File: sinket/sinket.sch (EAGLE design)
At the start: 16 parts, among them IC1 ATTINY85-20PU

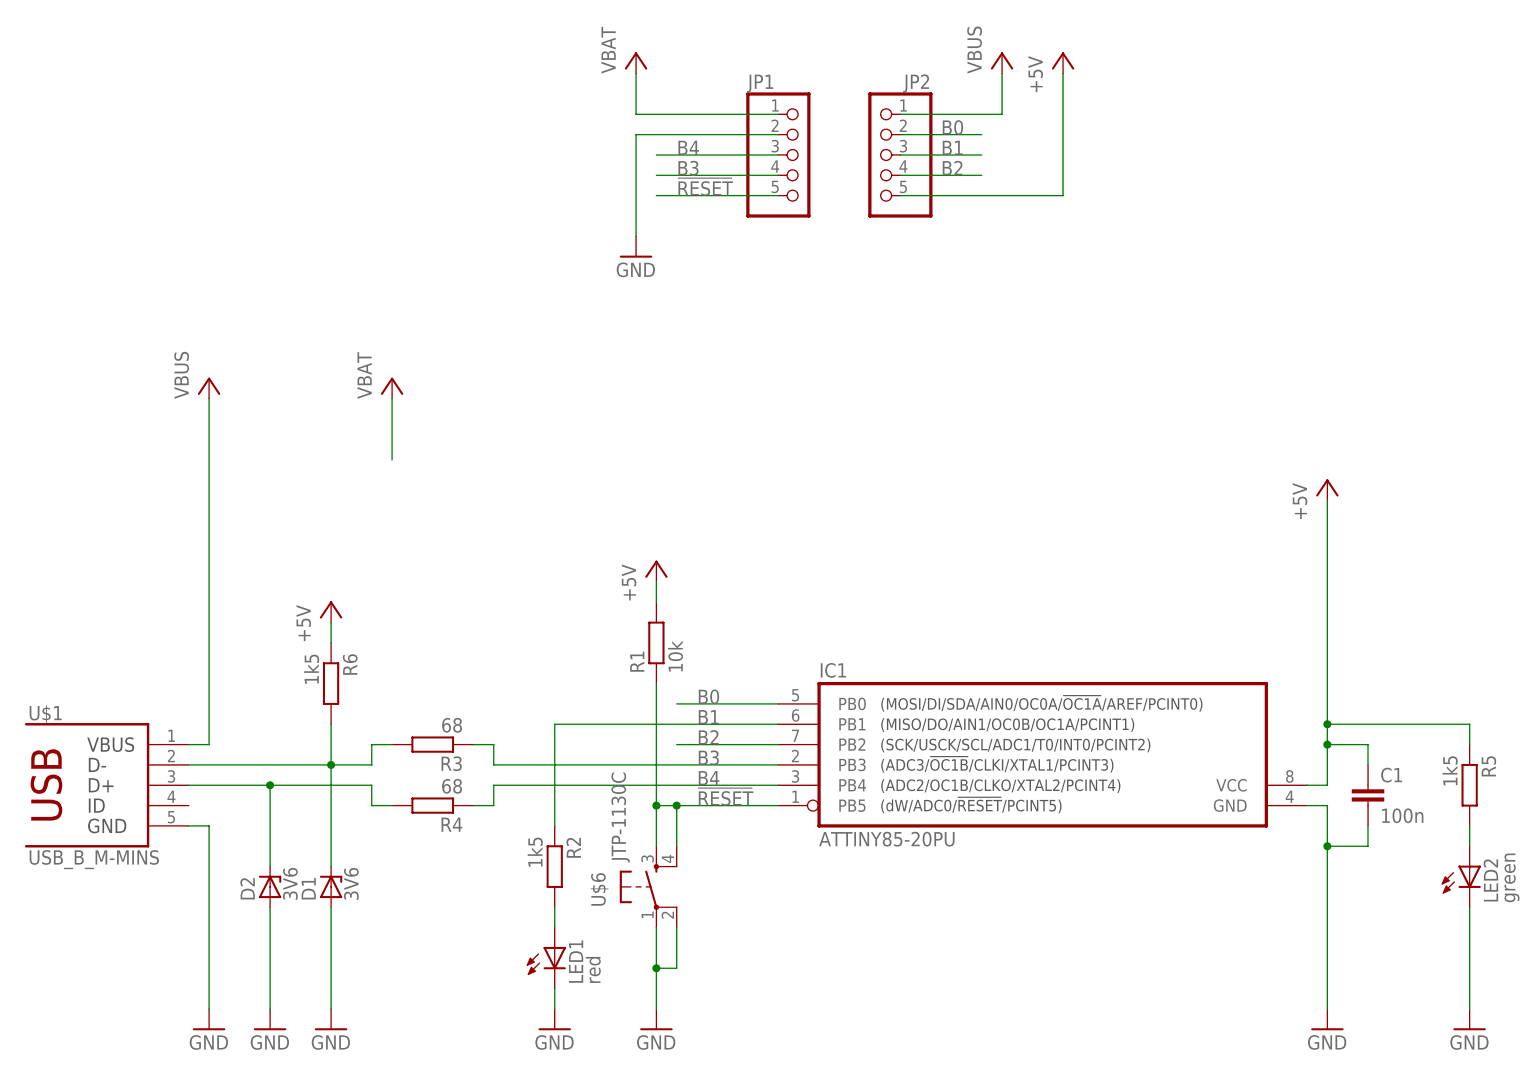
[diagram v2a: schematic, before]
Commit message: add remaining parts to schematic
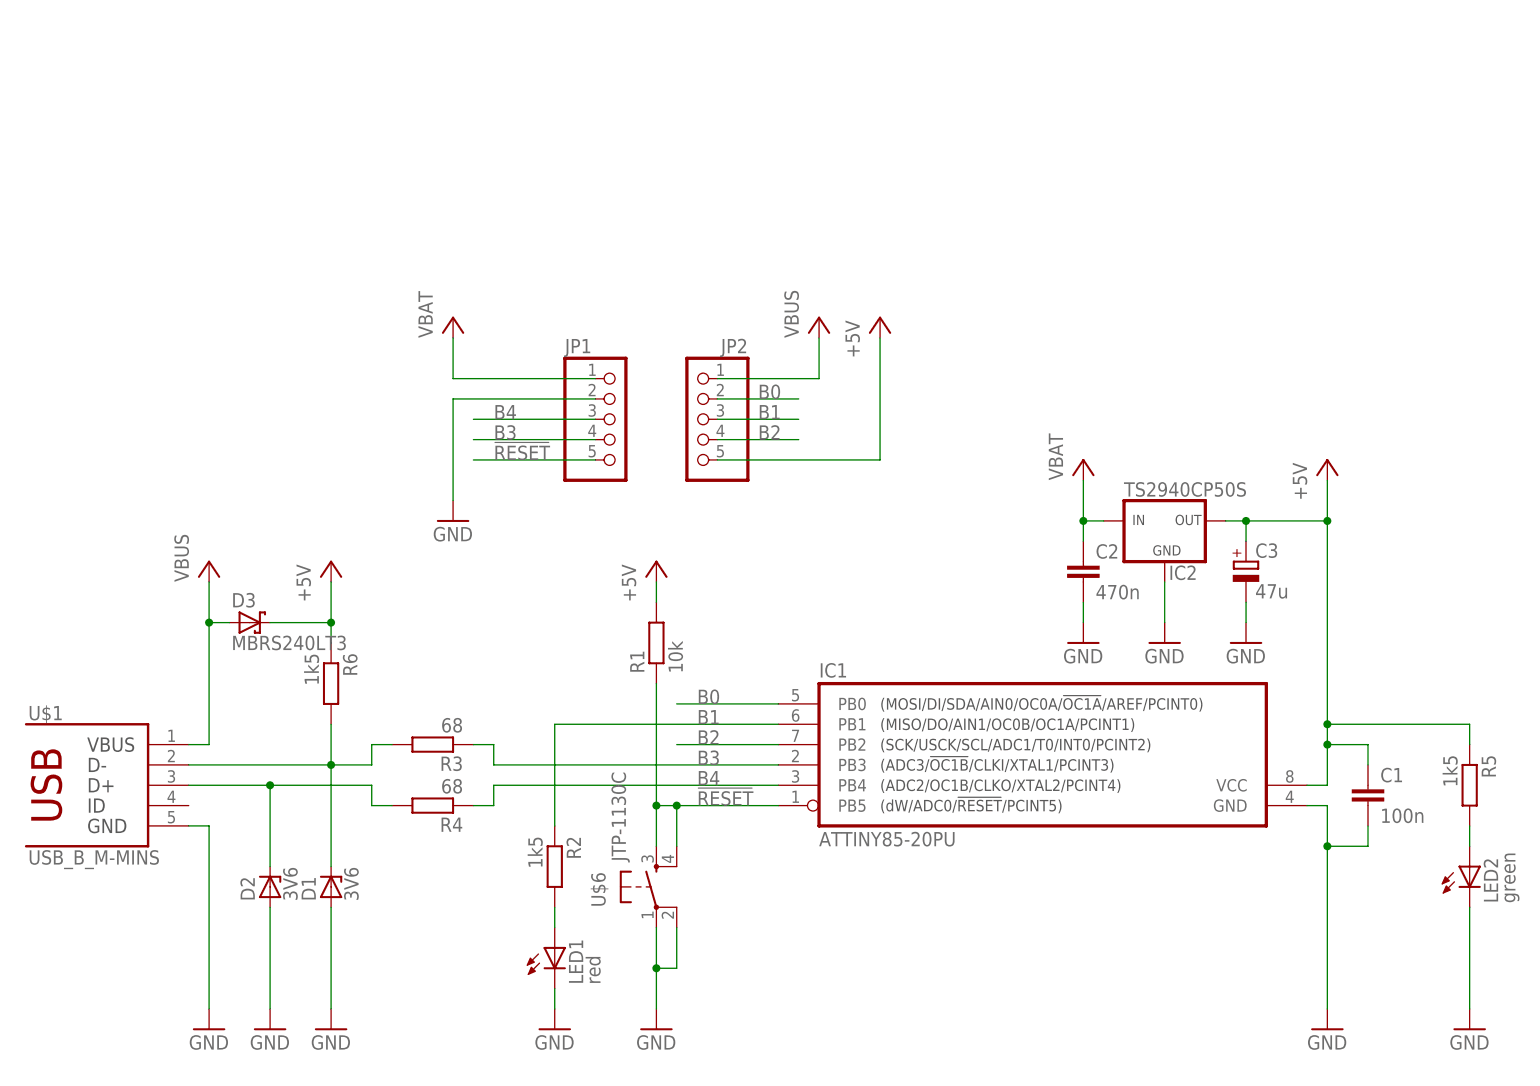
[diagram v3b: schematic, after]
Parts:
- added C2: 470n, rcl:C-EU025-030X050
- added C3: 47u, rcl:CPOL-EUE2.5-6
- added D3: MBRS240LT3, diode:MBRS130LT3
- added IC2: TS2940CP50S, n39:TS2940CP50S
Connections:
- net +5V: now also C3.+, D3.C, IC2.OUT
- net GND: now also C2.2, C3.-, IC2.GND
- net VBAT: now also C2.1, IC2.IN
- net VBUS: now also D3.A
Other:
- moved on the sheet: JP1, JP2
